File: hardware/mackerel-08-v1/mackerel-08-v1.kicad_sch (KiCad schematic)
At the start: 18 parts, among them J1 Conn_02x20_Odd_Even, U1 MC68008, U2 74HC595, U3 ATF22V10C, U4 ATF22V10C, U5 ATF22V10C, X1 CXO_DIP8

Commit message: Fixed most of the problems with rev 1
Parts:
- removed JP1: Jumper_2_Open, Connector_PinHeader_2.54mm:PinHeader_1x02_P2.54mm_Vertical, symbol Jumper:Jumper_2_Open
- removed X1: CXO_DIP8, Oscillator:Oscillator_DIP-8, symbol Oscillator:CXO_DIP8
- added J5: Conn_02x10_Odd_Even, Connector_PinHeader_2.54mm:PinHeader_2x10_P2.54mm_Vertical, symbol Connector_Generic:Conn_02x10_Odd_Even
- added R21: R, Resistor_THT:R_Axial_DIN0207_L6.3mm_D2.5mm_P7.62mm_Horizontal, symbol Device:R
- added X1: CXO_DIP14, Oscillator:Oscillator_DIP-14, symbol Oscillator:CXO_DIP14
- J1: footprint Connector_IDC:IDC-Header_2x20_P2.54mm_Vertical -> Connector_PinHeader_2.54mm:PinHeader_2x20_P2.54mm_Vertical
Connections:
- net +5V: now also J5.1 (Pin_1), J5.2 (Pin_2), R21.1, X1.14 (Vcc)
- net A16: now also J1.31 (Pin_31)
- net A17: now also J1.32 (Pin_32)
- net A18: now also J1.33 (Pin_33)
- net A19: now also J1.34 (Pin_34)
- net A20: now also J1.35 (Pin_35)
- net A21: now also J1.36 (Pin_36)
- net CLK_CPU: now also X1.8 (OUT)
- net GND: now also J5.19 (Pin_19), J5.20 (Pin_20), J5.3 (Pin_3), J5.4 (Pin_4), X1.7 (GND)
- net /AS: now also J5.5 (Pin_5); no longer J1.33 (Pin_33)
- net /DS: now also J5.6 (Pin_6); no longer J1.34 (Pin_34)
- net /DTACK_CPU: now also U5.23 (IO9)
- net /DTACK_EXP: now also J5.10 (Pin_10), R21.2; no longer J1.37 (Pin_37)
- net /EXP: now also J5.9 (Pin_9); no longer J1.35 (Pin_35)
- net /IACK_EXP: now also J5.12 (Pin_12); no longer J1.38 (Pin_38)
- net /IRQ_EXP: now also J5.11 (Pin_11); no longer J1.36 (Pin_36)
- net /RESET: now also J1.37 (Pin_37), J1.38 (Pin_38); no longer J1.31 (Pin_31)
- net /RW: now also J5.7 (Pin_7); no longer J1.32 (Pin_32)
- net /VPA: now reaches R7.1, U1.43 (/VPA)
- net /VPA: now also J5.8 (Pin_8)
- new net SPI_CLK: J5.15 (Pin_15)
- new net SPI_CS: J5.16 (Pin_16)
- new net SPI_DI: J5.13 (Pin_13)
- new net SPI_DO: J5.14 (Pin_14)
- new net SPI_INT: J5.17 (Pin_17)
- new net X_OUT: J5.18 (Pin_18)
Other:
- note removed: "Open for DTACK grounded Closed for DTACK control"
- moved on the sheet: R1, R2, R3, R4, R5, R6, R7, U1

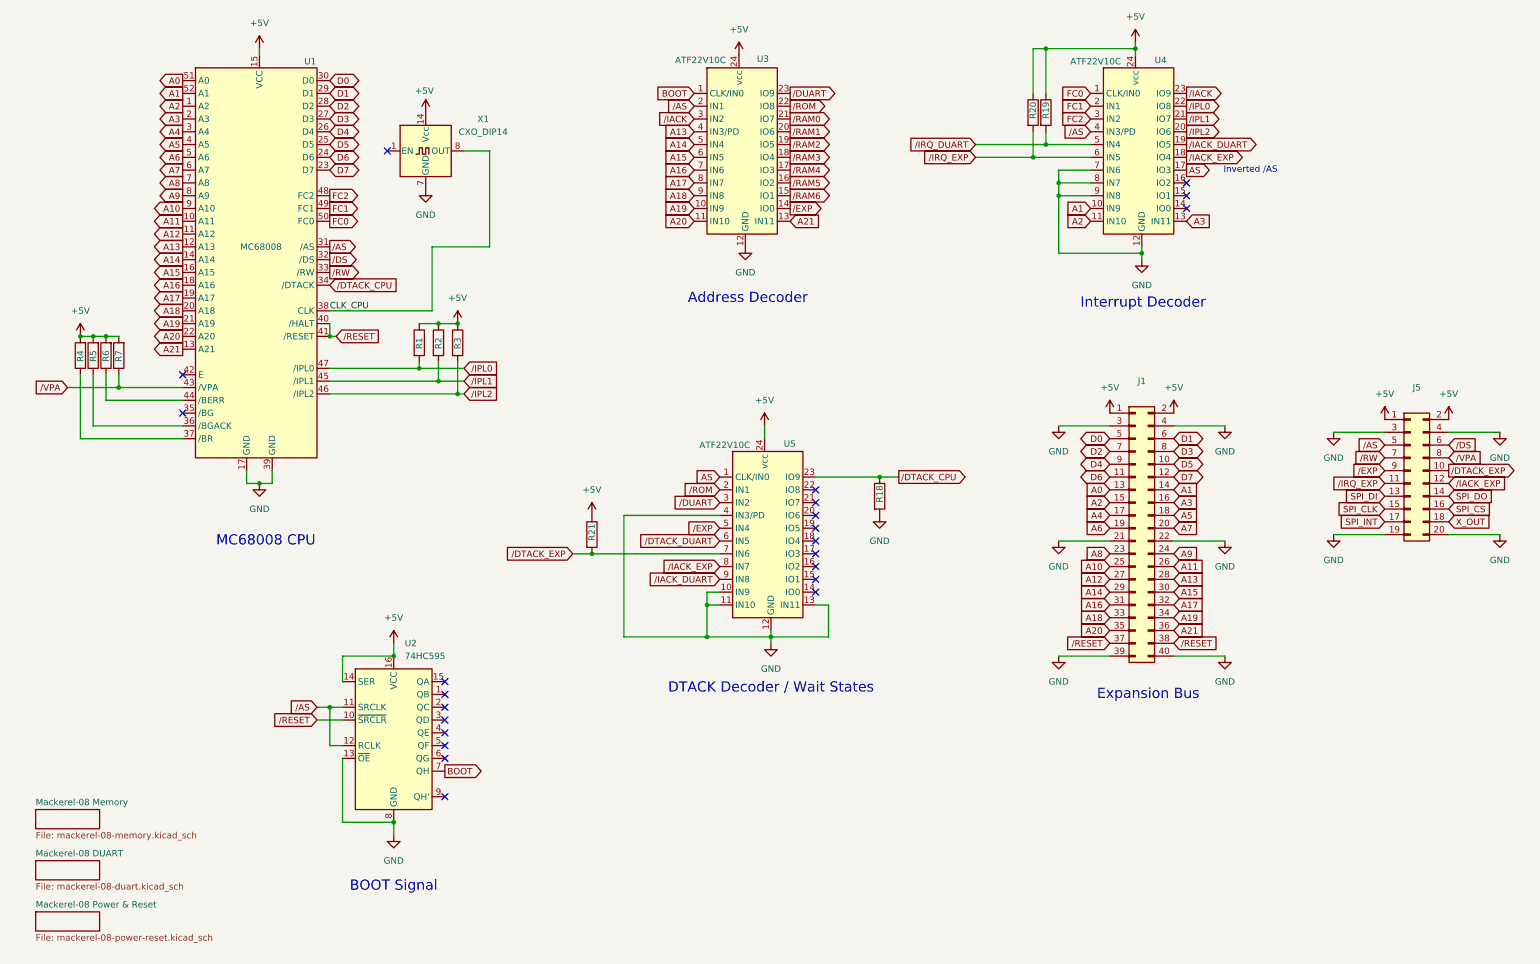
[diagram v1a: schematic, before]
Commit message: Mack-08 1.1 schematic fixes done, needs final routing
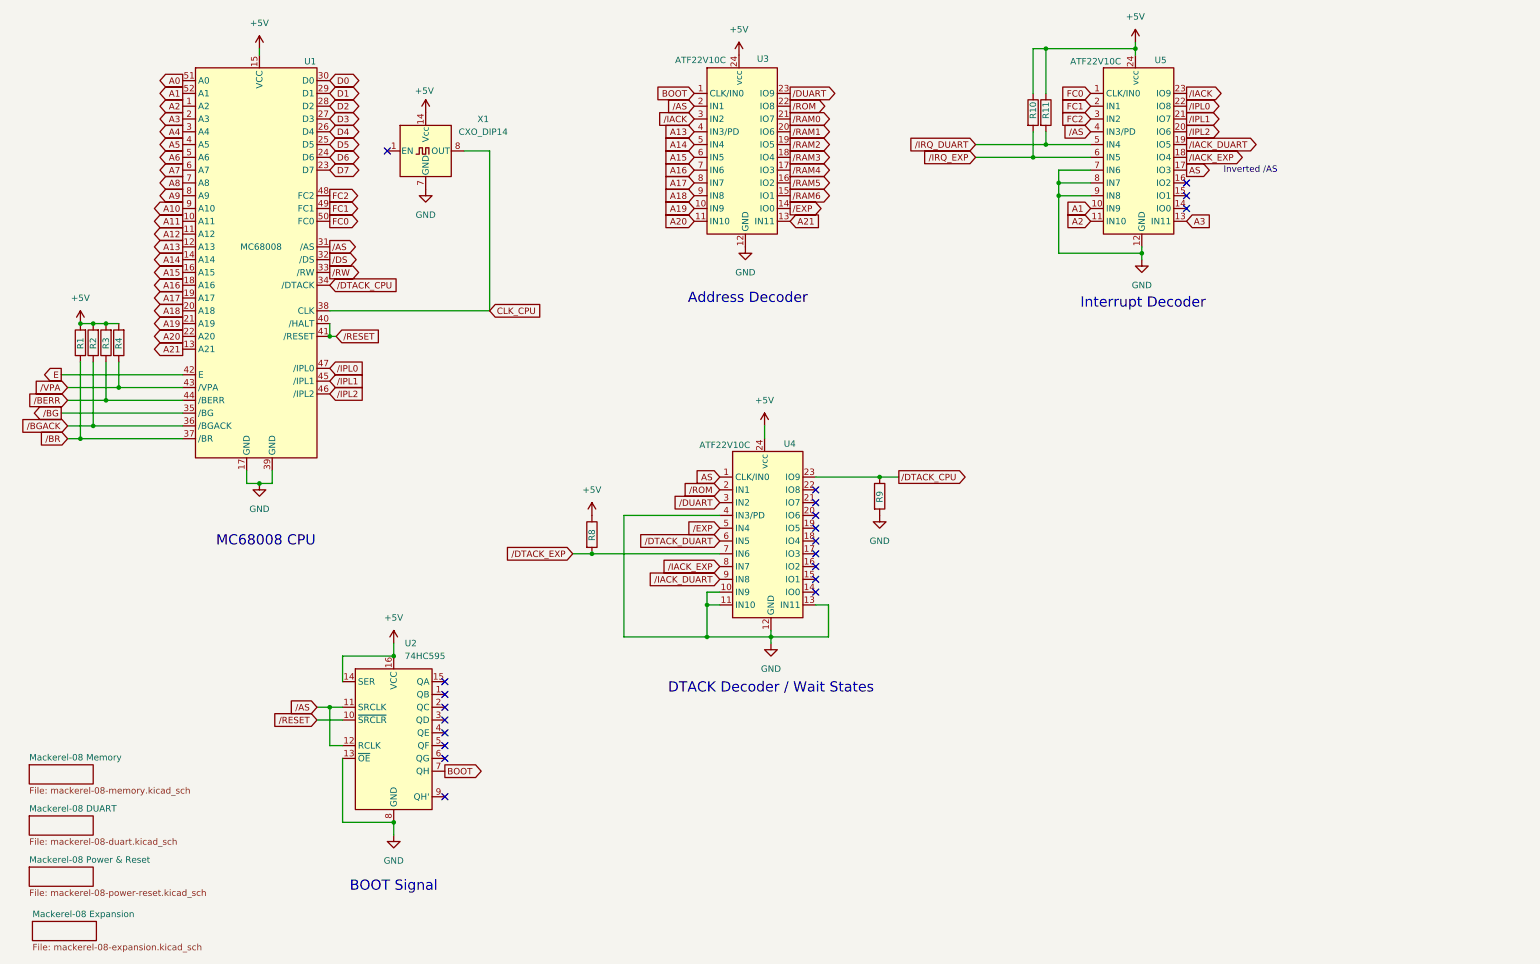
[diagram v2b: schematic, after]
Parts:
- removed J1: Conn_02x20_Odd_Even, Connector_PinHeader_2.54mm:PinHeader_2x20_P2.54mm_Vertical, symbol Connector_Generic:Conn_02x20_Odd_Even
- removed J5: Conn_02x10_Odd_Even, Connector_PinHeader_2.54mm:PinHeader_2x10_P2.54mm_Vertical, symbol Connector_Generic:Conn_02x10_Odd_Even
- removed R1, R2, R3: R, Resistor_THT:R_Axial_DIN0207_L6.3mm_D2.5mm_P7.62mm_Horizontal, symbol Device:R
- renumbered R4 to R1, R20 to R10, R19 to R11, R5 to R2, R6 to R3, R7 to R4, R21 to R8, R18 to R9, U5 to U4, U4 to U5
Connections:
- net /BGACK: now reaches R2.1, U1.36 (/BGACK)
- net /BR: now reaches R1.1, U1.37 (/BR)
- net /BG: now reaches U1.35 (/BG)
- net E: now reaches U1.42 (E)
- net /BERR: now reaches R3.1, U1.44 (/BERR)
- no-connect marks 23 -> 21
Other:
- added sheet Mackerel-08 Expansion (mackerel-08-expansion.kicad_sch)
- note removed: "Expansion Bus"
- moved on the sheet: R1, R2, R3, R4

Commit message: Mack-08 rev 1.1 routed
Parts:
- added R5, R6, R7: R, Resistor_SMD:R_1206_3216Metric_Pad1.30x1.75mm_HandSolder, symbol Device:R
- R1, R10, R11, R2, R3, R4, R8, R9: footprint Resistor_THT:R_Axial_DIN0207_L6.3mm_D2.5mm_P7.62mm_Horizontal -> Resistor_SMD:R_1206_3216Metric_Pad1.30x1.75mm_HandSolder
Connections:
- net +5V: now also R5.2, R6.2, R7.2
- net /IPL0: now also R5.1
- net /IPL1: now also R6.1
- net /IPL2: now also R7.1

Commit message: Mackerel-08 v1.1 release
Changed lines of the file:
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@@
 	)
 	(sheet
-		(at 15.875 193.675)
+		(at 15.24 193.675)
 		(size 12.7 3.81)
 		(fields_autoplaced yes)
@@
 		)
 		(property "Sheetname" "Mackerel-08 Expansion"
-			(at 15.875 192.9634 0)
+			(at 15.24 192.9634 0)
 			(effects
 				(font
@@
 		)
 		(property "Sheetfile" "mackerel-08-expansion.kicad_sch"
-			(at 15.875 198.0696 0)
+			(at 15.24 198.0696 0)
 			(effects
 				(font

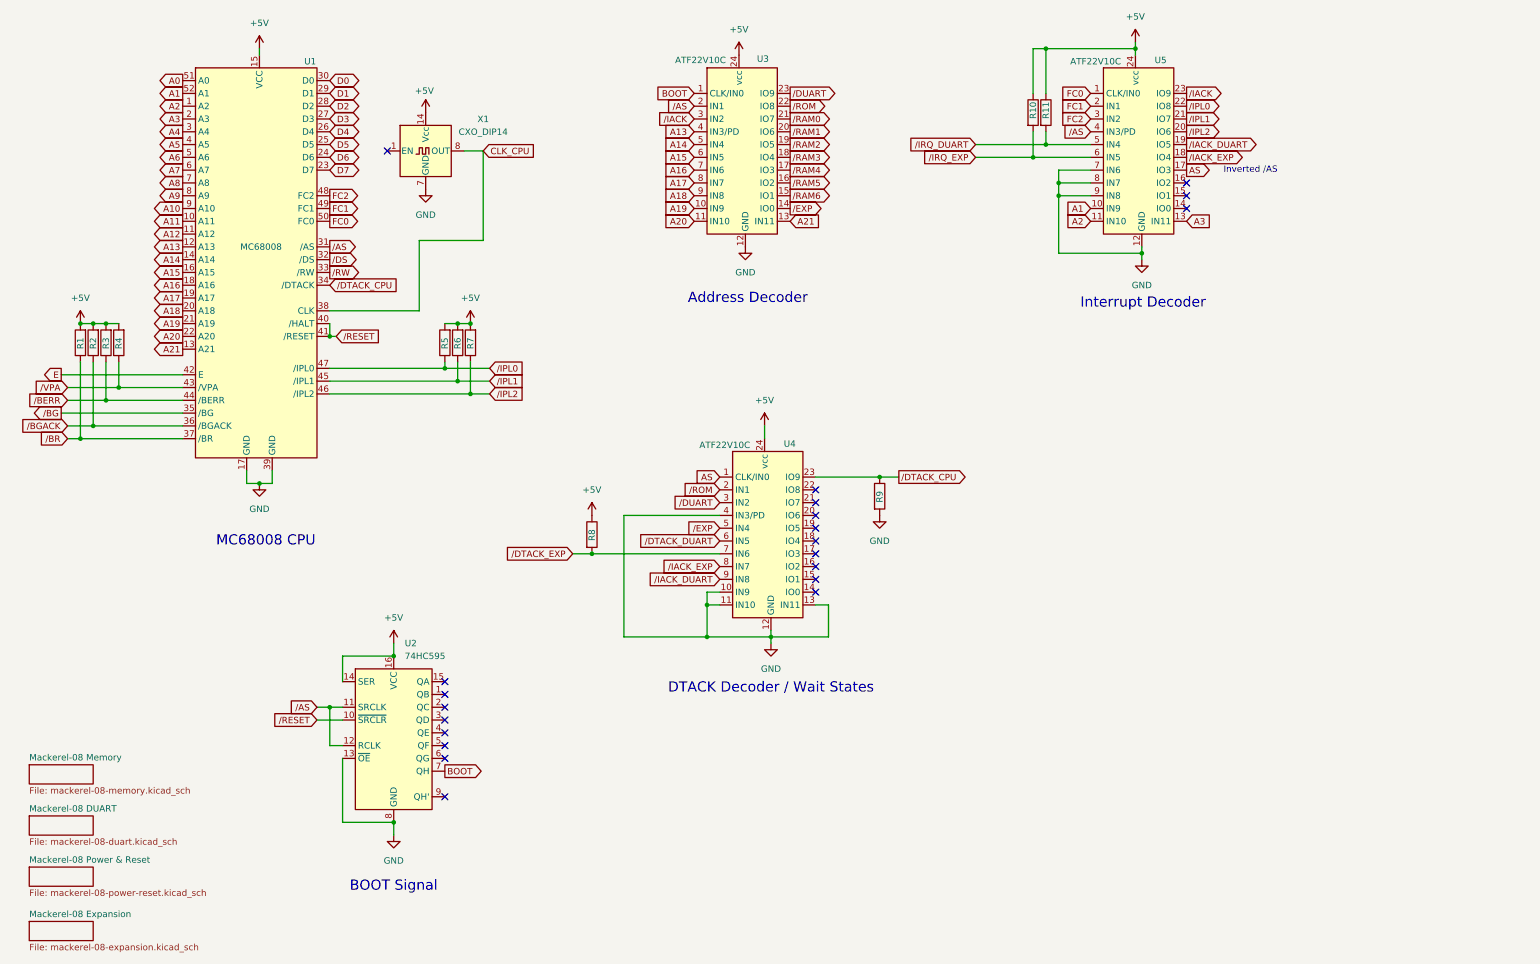
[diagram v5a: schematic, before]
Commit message: Add Mackerel-08 BOM list
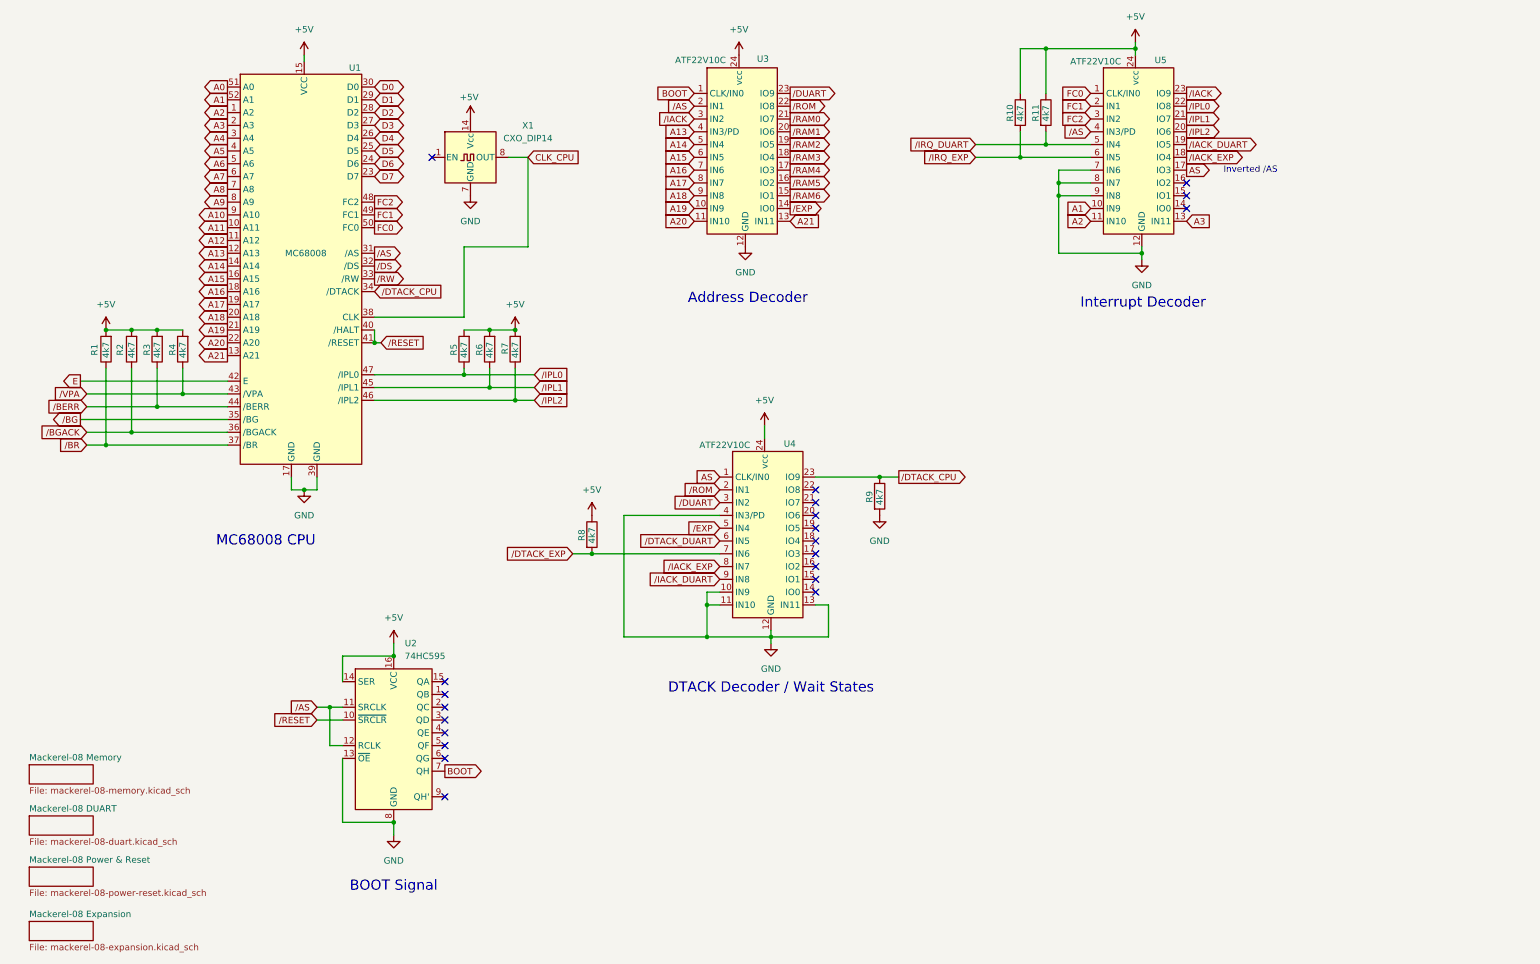
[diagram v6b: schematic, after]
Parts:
- R1, R10, R11, R2, R3, R4, R5, R6, R7, R8, R9: value R -> 4k7
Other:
- title: Mackerel-08 SBC v1 -> Mackerel-08 SBC v1.1
- moved on the sheet: R1, R10, R2, R3, R4, R5, R6, R7, U1, X1
